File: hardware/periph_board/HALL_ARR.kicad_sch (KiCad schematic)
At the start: 24 parts, among them U200 AH49HNTR-G1, U201 AH49HNTR-G1, U202 AH49HNTR-G1, U203 AH49HNTR-G1, U204 AH49HNTR-G1, U205 AH49HNTR-G1, U206 AH49HNTR-G1, U207 AH49HNTR-G1, U208 AH49HNTR-G1, U209 AH49HNTR-G1, U210 AH49HNTR-G1, U211 AH49HNTR-G1

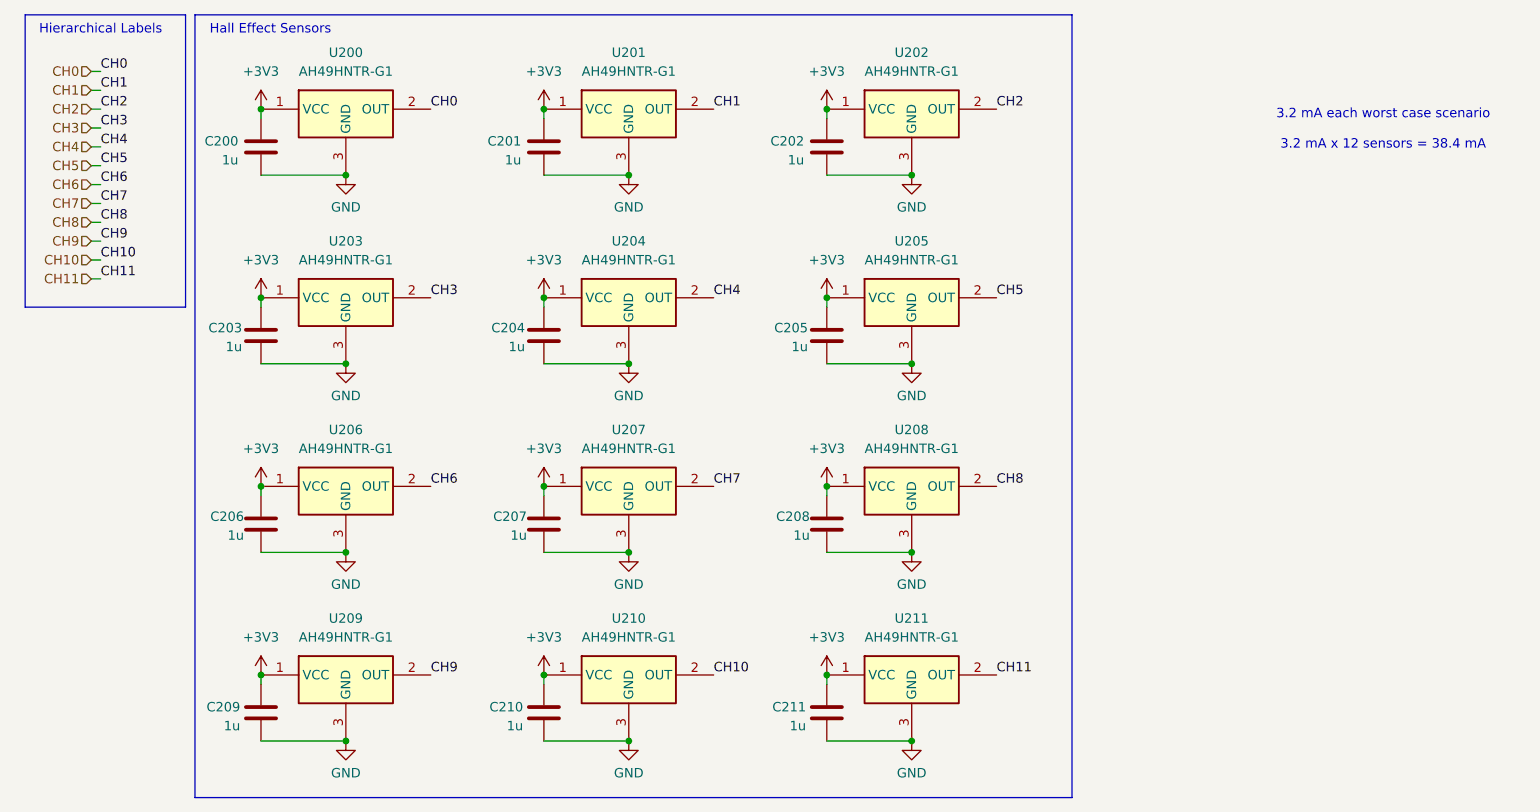
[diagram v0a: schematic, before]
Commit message: Adjusted spacing to 13.5mm between hall effects
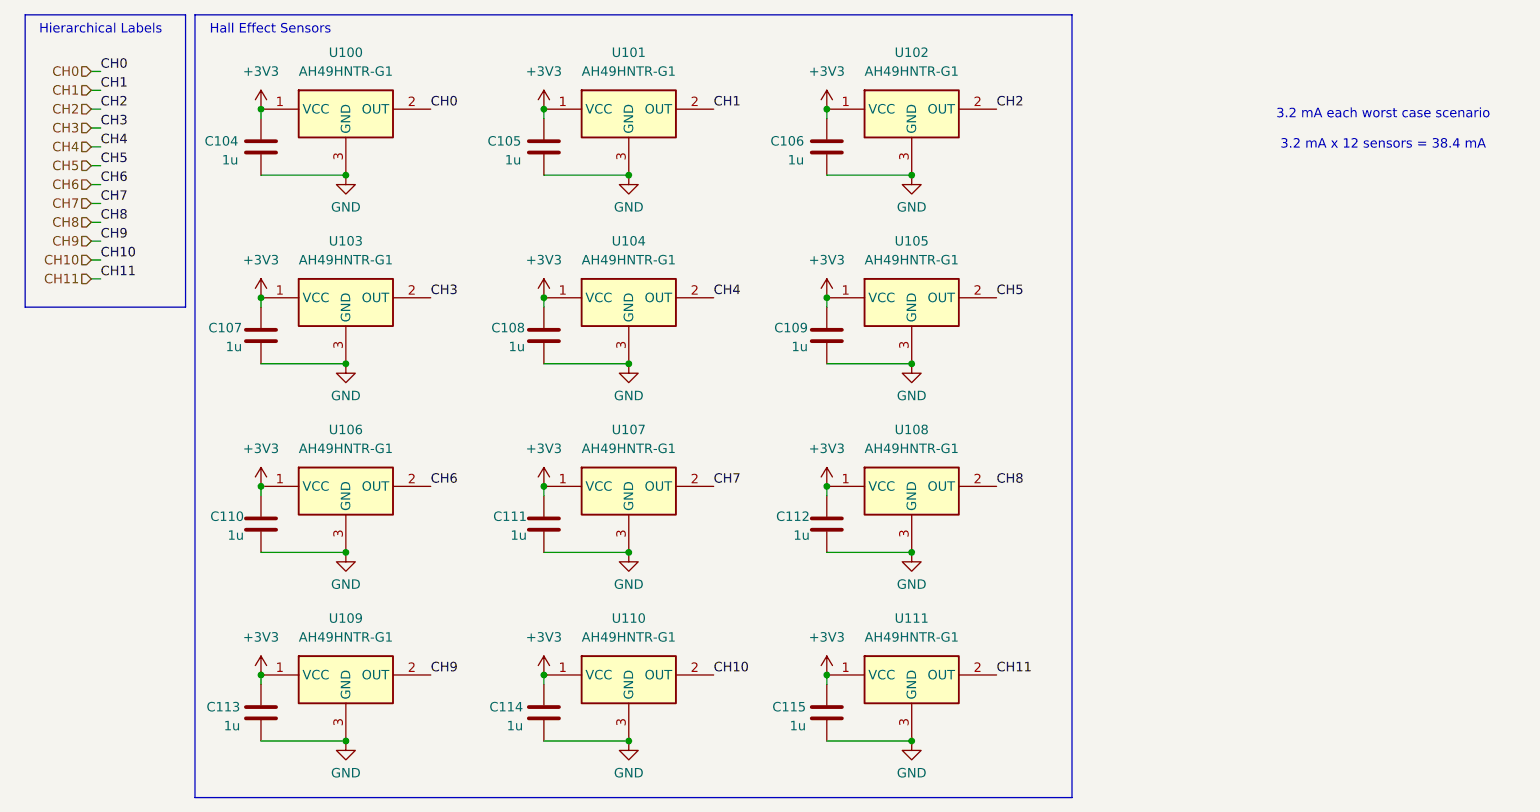
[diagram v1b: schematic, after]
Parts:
- renumbered C200 to C104, C201 to C105, C202 to C106, C203 to C107, C204 to C108, C205 to C109, C206 to C110, C207 to C111, C208 to C112, C209 to C113, C210 to C114, C211 to C115, U200 to U100, U201 to U101, U202 to U102, U203 to U103, U204 to U104, U205 to U105, U206 to U106, U207 to U107, U208 to U108, U209 to U109, U210 to U110, U211 to U111
